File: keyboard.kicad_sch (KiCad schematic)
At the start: 104 parts

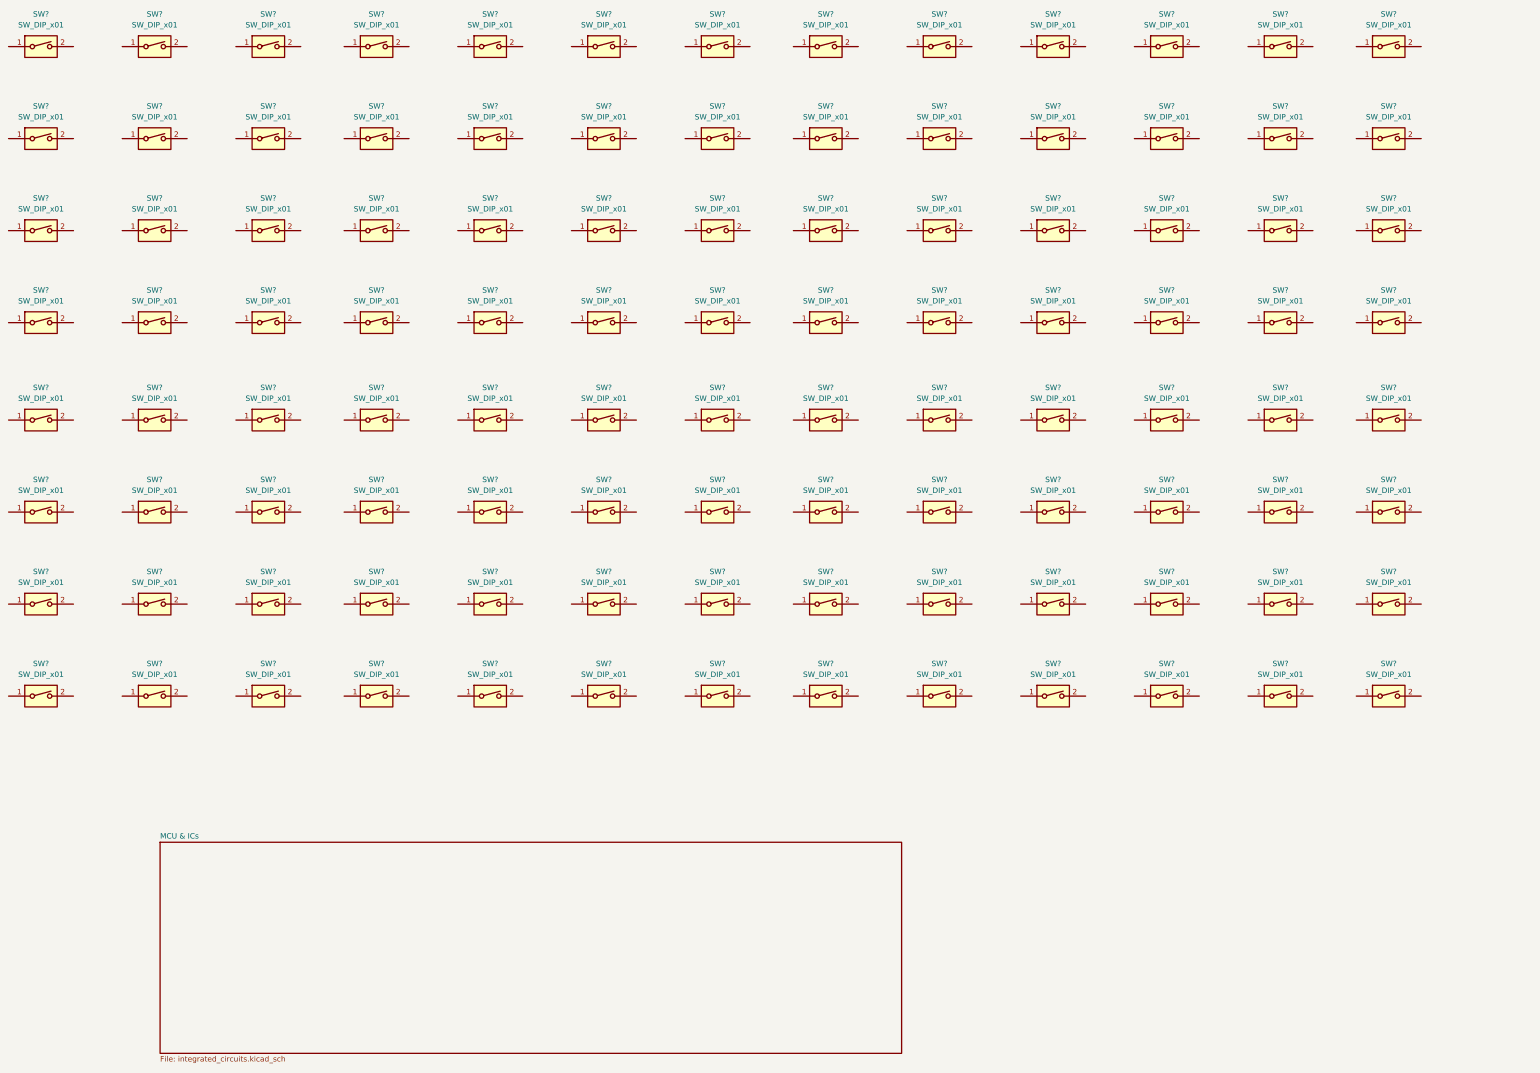
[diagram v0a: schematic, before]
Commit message: Add row connections with heirarchical labels
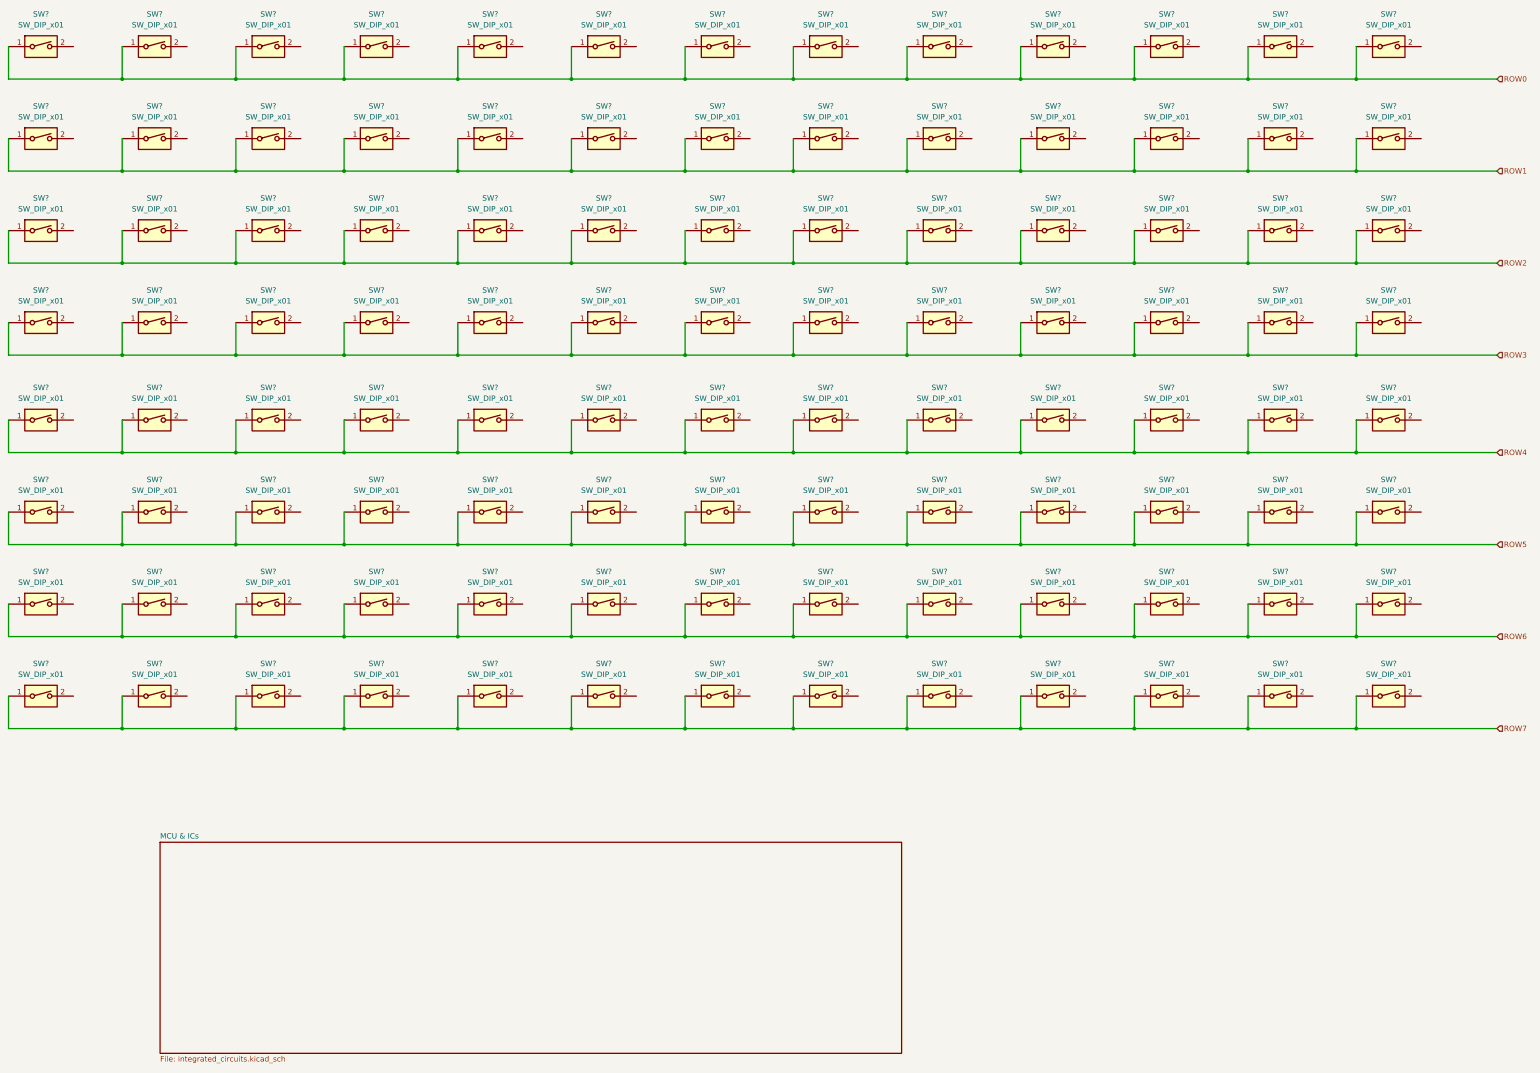
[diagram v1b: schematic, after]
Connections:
- net ROW7: now reaches SW?.1
- net ROW7: now also SW?.1, SW?.1, SW?.1, SW?.1, SW?.1, SW?.1, SW?.1, SW?.1, SW?.1, SW?.1, SW?.1, SW?.1
- net ROW6: now reaches SW?.1
- net ROW6: now also SW?.1, SW?.1, SW?.1, SW?.1, SW?.1, SW?.1, SW?.1, SW?.1, SW?.1, SW?.1, SW?.1, SW?.1
- net ROW5: now reaches SW?.1
- net ROW5: now also SW?.1, SW?.1, SW?.1, SW?.1, SW?.1, SW?.1, SW?.1, SW?.1, SW?.1, SW?.1, SW?.1, SW?.1
- net ROW0: now reaches SW?.1
- net ROW0: now also SW?.1, SW?.1, SW?.1, SW?.1, SW?.1, SW?.1, SW?.1, SW?.1, SW?.1, SW?.1, SW?.1, SW?.1
- net ROW1: now reaches SW?.1
- net ROW1: now also SW?.1, SW?.1, SW?.1, SW?.1, SW?.1, SW?.1, SW?.1, SW?.1, SW?.1, SW?.1, SW?.1, SW?.1
- net ROW2: now reaches SW?.1
- net ROW2: now also SW?.1, SW?.1, SW?.1, SW?.1, SW?.1, SW?.1, SW?.1, SW?.1, SW?.1, SW?.1, SW?.1, SW?.1
- net ROW3: now reaches SW?.1
- net ROW3: now also SW?.1, SW?.1, SW?.1, SW?.1, SW?.1, SW?.1, SW?.1, SW?.1, SW?.1, SW?.1, SW?.1, SW?.1
- net ROW4: now reaches SW?.1
- net ROW4: now also SW?.1, SW?.1, SW?.1, SW?.1, SW?.1, SW?.1, SW?.1, SW?.1, SW?.1, SW?.1, SW?.1, SW?.1
